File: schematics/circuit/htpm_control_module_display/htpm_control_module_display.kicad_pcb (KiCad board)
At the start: 2 copper layers, 73.7 x 48.3 mm, 58 parts, among them J1 Conn_01x10_Socket, J2 Conn_01x10_Socket

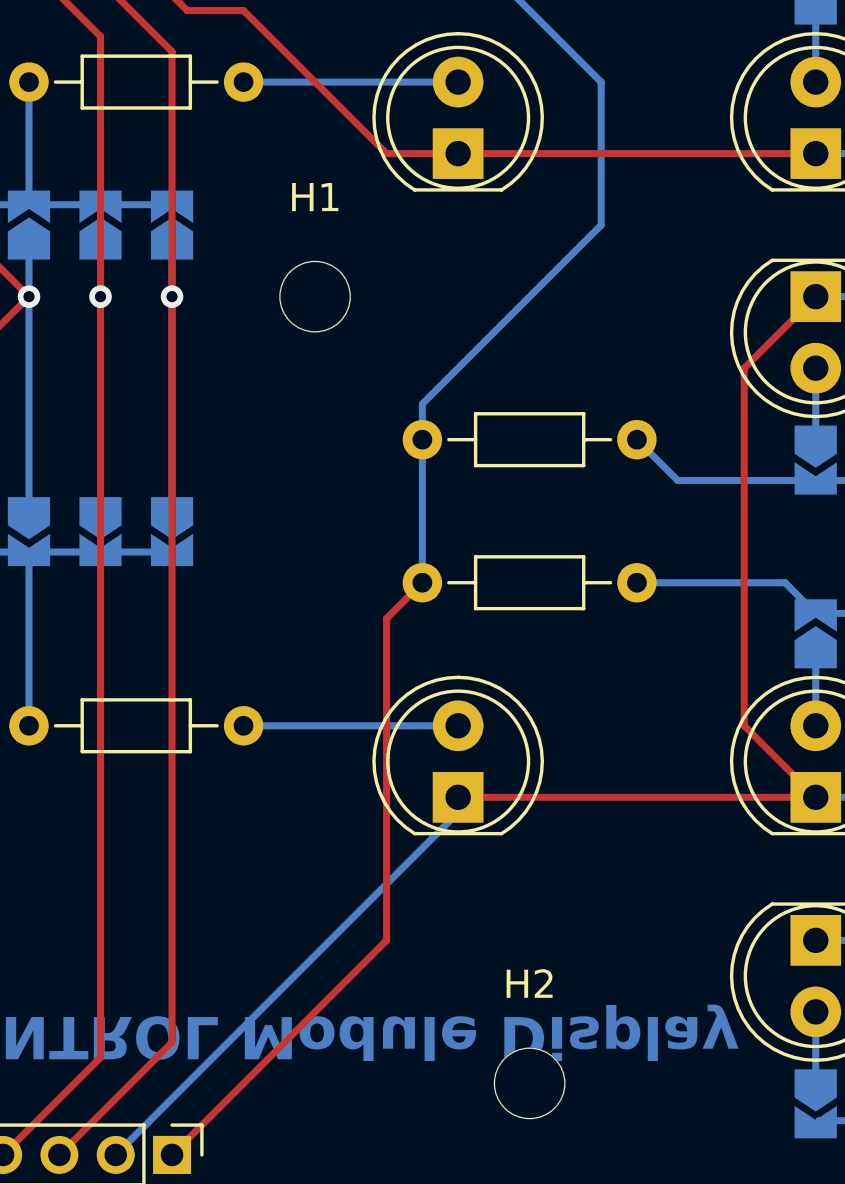
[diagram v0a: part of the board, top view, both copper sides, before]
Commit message: Updated comments on the HTPm CONTROL Module Display.
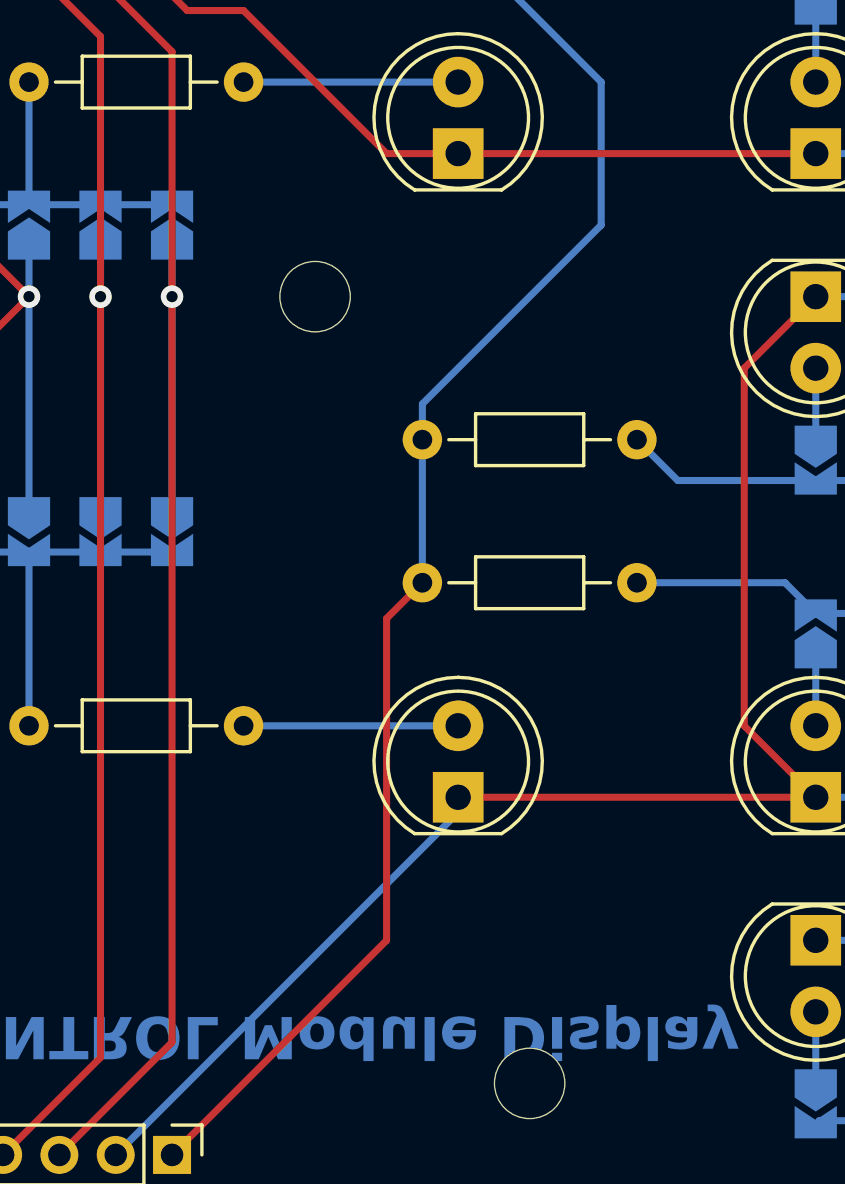
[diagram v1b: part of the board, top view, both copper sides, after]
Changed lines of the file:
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@@
   (paper "A4")
   (title_block
-    (title "HTP!m CONTROL Display")
+    (title "HTP!m CONTROL Module Display")
     (date "2023-10-07")
     (rev "1")
     (company "shawnd.xyz")
-    (comment 2 "to the user.")
-    (comment 3 "The HTP!m CONTROL display panel is a series of LED matrices that communicate data")
+    (comment 2 "status.")
+    (comment 3 "The HTP!m CONTROL Module Display highlights the selected module and its override")
   )
   (layers
@@
     (property "ki_keywords" "mounting hole")
     (attr exclude_from_pos_files)
-    (fp_text reference "H2" (at 0 -3.5) (layer "F.SilkS")
-        (effects (font (size 1 1) (thickness 0.15)))
+    (fp_text reference "H2" (at 0 -3.5) (layer "B.SilkS")
+        (effects (font (size 1 1) (thickness 0.15)) (justify mirror))
     )
     (fp_text value "MountingHole" (at 0 3.5) (layer "F.Fab")
@@
     (property "ki_keywords" "mounting hole")
     (attr exclude_from_pos_files)
-    (fp_text reference "H1" (at 0 -3.5) (layer "F.SilkS")
-        (effects (font (size 1 1) (thickness 0.15)))
+    (fp_text reference "H1" (at 0 -3.5) (layer "B.SilkS")
+        (effects (font (size 1 1) (thickness 0.15)) (justify mirror))
     )
     (fp_text value "MountingHole" (at 0 3.5) (layer "F.Fab")
